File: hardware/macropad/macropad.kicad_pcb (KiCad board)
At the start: 2 copper layers, 13 parts, among them J2 Conn_01x04_Pin, SW1 SW_Push, SW2 SW_Push, SW3 SW_Push, SW4 SW_Push, SW5 SW_Push, SW6 SW_Push, SW7 SW_Push, SW8 SW_Push, SW9 SW_Push, U1 NRF24L01_Breakout, U2 AP2112K-3.3, U3 STM32F103C8Tx

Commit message: schematic halfass done
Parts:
- added C10: 10u, Capacitor_SMD:C_0805_2012Metric, F.Cu at (42.5, 65.8)
- added C11: 12p, Capacitor_SMD:C_0805_2012Metric, F.Cu at (42.5, 68.8)
- added C12: 100n, Capacitor_SMD:C_0805_2012Metric, F.Cu at (42.5, 71.8)
- added C13: 1u, Capacitor_SMD:C_0805_2012Metric, F.Cu at (42.5, 74.8)
- added C14: 100n, Capacitor_SMD:C_0805_2012Metric, F.Cu at (47.0, 65.8)
- added C15: 12p, Capacitor_SMD:C_0805_2012Metric, F.Cu at (47.0, 68.8)
- added C16: 100n, Capacitor_SMD:C_0805_2012Metric, F.Cu at (47.0, 71.8)
- added C17: 100n, Capacitor_SMD:C_0805_2012Metric, F.Cu at (47.0, 74.8)
- added C18: 1u, Capacitor_SMD:C_0805_2012Metric, F.Cu at (51.4, 65.8)
- added C19: 100n, Capacitor_SMD:C_0805_2012Metric, F.Cu at (51.4, 68.8)
- added C20: 100n, Capacitor_SMD:C_0805_2012Metric, F.Cu at (51.4, 71.8)
- added C21: 10u, Capacitor_SMD:C_0805_2012Metric, F.Cu at (51.4, 74.8)
- added J1: Conn_01x04_Pin, Connector_PinHeader_2.54mm:PinHeader_1x04_P2.54mm_Horizontal, F.Cu at (85.9, 52.3)
- added J3: Conn_02x03_Counter_Clockwise, Connector_PinHeader_2.54mm:PinHeader_1x04_P2.54mm_Vertical, F.Cu at (108.5, 116.6)
- added J4: display(4x1), Connector_PinHeader_2.54mm:PinHeader_1x04_P2.54mm_Vertical, F.Cu at (108.5, 101.9)
- added J5: enc1, Connector_PinHeader_2.54mm:PinHeader_1x05_P2.54mm_Horizontal, F.Cu at (121.9, 101.9)
- added J6: enc2, Connector_PinHeader_2.54mm:PinHeader_1x05_P2.54mm_Horizontal, F.Cu at (85.9, 37.6)
- added J7: Conn_01x04_Pin, Connector_PinHeader_2.54mm:PinHeader_1x04_P2.54mm_Horizontal, F.Cu at (42.6, 54.4)
- added J8: USB_A, Connector_USB:USB_A_Connfly_DS1095, F.Cu at (27.5, 54.2)
- added J9: Conn_02x03_Counter_Clockwise, Connector_PinHeader_2.54mm:PinHeader_2x03_P2.54mm_Vertical, F.Cu at (55.9, 66.6)
- added R11: 1.5K, Resistor_SMD:R_0805_2012Metric, F.Cu at (34.3, 69.7)
- added R12: 10k, Resistor_SMD:R_0805_2012Metric, F.Cu at (34.3, 72.7)
- added SW10: SW_Push, keyswitches:Kailh_socket_MX, F.Cu at (75.4, 43.4)
- added SW11: SW_Push, keyswitches:Kailh_socket_MX, F.Cu at (75.4, 59.5)
- added SW12: SW_Push, Button_Switch_SMD:SW_DIP_SPSTx01_Slide_6.7x4.1mm_W6.73mm_P2.54mm_LowProfile_JPin, F.Cu at (26.8, 71.1)
- added U4: AP2112K-3.3, Package_TO_SOT_SMD:SOT-23-5, F.Cu at (56.2, 59.0)
- added U5: STM32F103C8Tx, Package_QFP:LQFP-48_7x7mm_P0.5mm, F.Cu at (58.3, 41.0)
- added U6: NRF24L01_Breakout, RF_Module:nRF24L01_Breakout, F.Cu at (24.3, 38.1)
- added Y1: 8Mhz, Crystal:Crystal_SMD_3225-4Pin_3.2x2.5mm, F.Cu at (56.3, 54.4)
- J2: value Conn_01x04_Pin -> USB_B_Micro; footprint Connector:Tag-Connect_TC2030-IDC-NL_2x03_P1.27mm_Vertical -> Connector_PinHeader_2.54mm:PinHeader_1x04_P2.54mm_Horizontal
- SW1: value SW_Push -> SW_SPDT
- U1: value NRF24L01_Breakout -> AP2112K-3.3; footprint RF_Module:nRF24L01_Breakout -> Package_TO_SOT_SMD:SOT-23-5
- U2: value AP2112K-3.3 -> STM32F103C8Tx; footprint Package_TO_SOT_SMD:SOT-23-5 -> Package_QFP:LQFP-48_7x7mm_P0.5mm
- U3: value STM32F103C8Tx -> NRF24L01_Breakout; footprint Package_QFP:LQFP-48_7x7mm_P0.5mm -> RF_Module:nRF24L01_Breakout
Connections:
- J2 pad 1: +3.3V -> VBUS
- J2 pad 2: /SWDIO -> /USB_D-
- J2 pad 3: /SWCLK -> /USB_D+
- J2 pad 4: GND -> unconnected-(J2-ID-Pad4)
- SW1 pad 1: GND -> /BAT_OUT_ON
- SW1 pad 2: /K1 -> /BAT_OUT
- SW2 pad 1: GND -> /NRST
- SW2 pad 2: /K2 -> GND
- SW3 pad 2: /K4 -> /K1
- SW4 pad 2: /K5 -> /K4
- SW5 pad 2: /K6 -> /K7
- SW6 pad 2: /K3 -> /K2
- SW7 pad 2: /K7 -> /K5
- SW9 pad 2: /K9 -> /K3
- U1 pad 1: GND -> VDD
- U1 pad 2: +3.3V -> GND
- U1 pad 3: /PB1 -> unconnected-(U1-EN-Pad3)
- U1 pad 4: /PB0 -> unconnected-(U1-NC-Pad4)
- U1 pad 5: /PA5 -> +3.3V
- U2 pad 1: VDD -> unconnected-(U2-VBAT-Pad1)
- U2 pad 2: GND -> /K1
- U2 pad 3: unconnected-(U2-EN-Pad3) -> /K2
- U2 pad 4: unconnected-(U2-NC-Pad4) -> /K3
- U2 pad 5: +3.3V -> unconnected-(U2-PD0-Pad5)
- U3 pad 1: unconnected-(U3-VBAT-Pad1) -> GND
- U3 pad 2: /K1 -> +3.3V
- U3 pad 3: /K2 -> /PB1
- U3 pad 4: /K3 -> /PB0
- U3 pad 5: unconnected-(U3-PD0-Pad5) -> /PA5
- U3 pad 6: unconnected-(U3-PD1-Pad6) -> /PA7
- U3 pad 7: unconnected-(U3-NRST-Pad7) -> /PA6
- U3 pad 8: GND -> /PB10

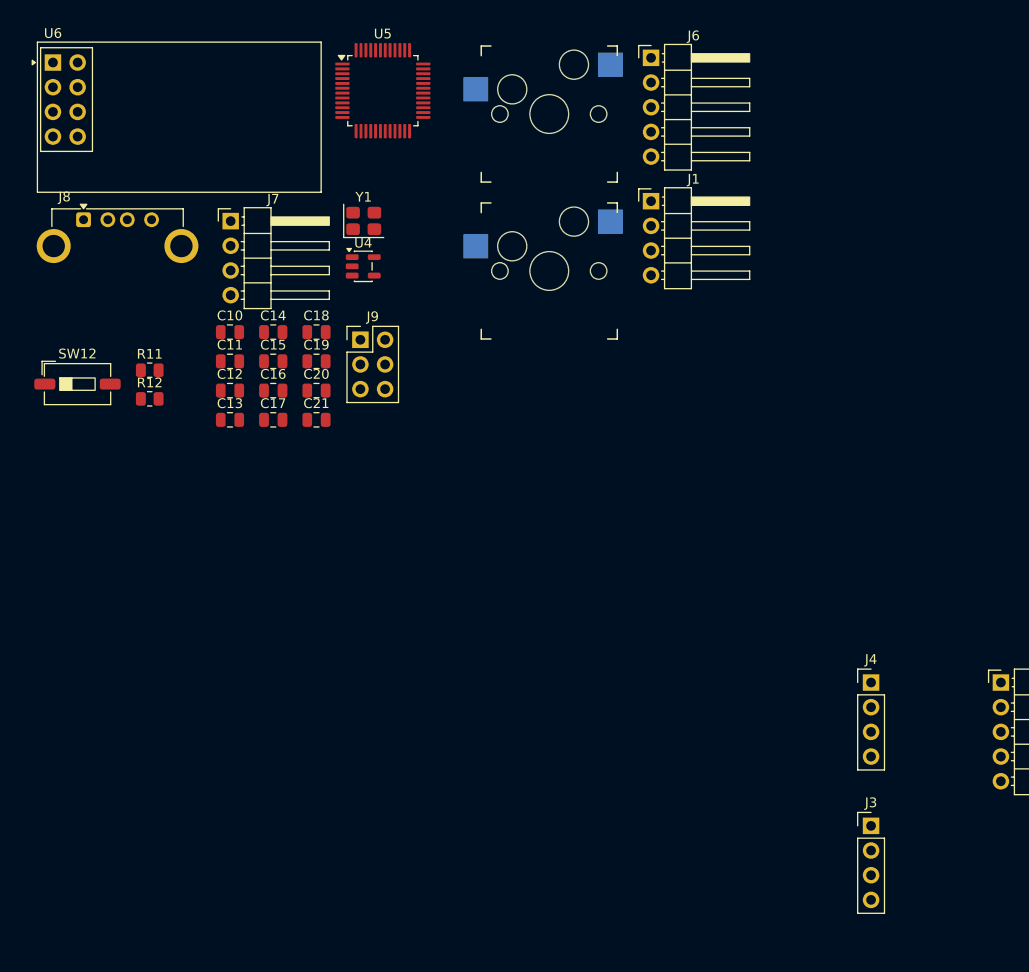
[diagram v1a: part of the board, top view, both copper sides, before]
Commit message: updated footprints
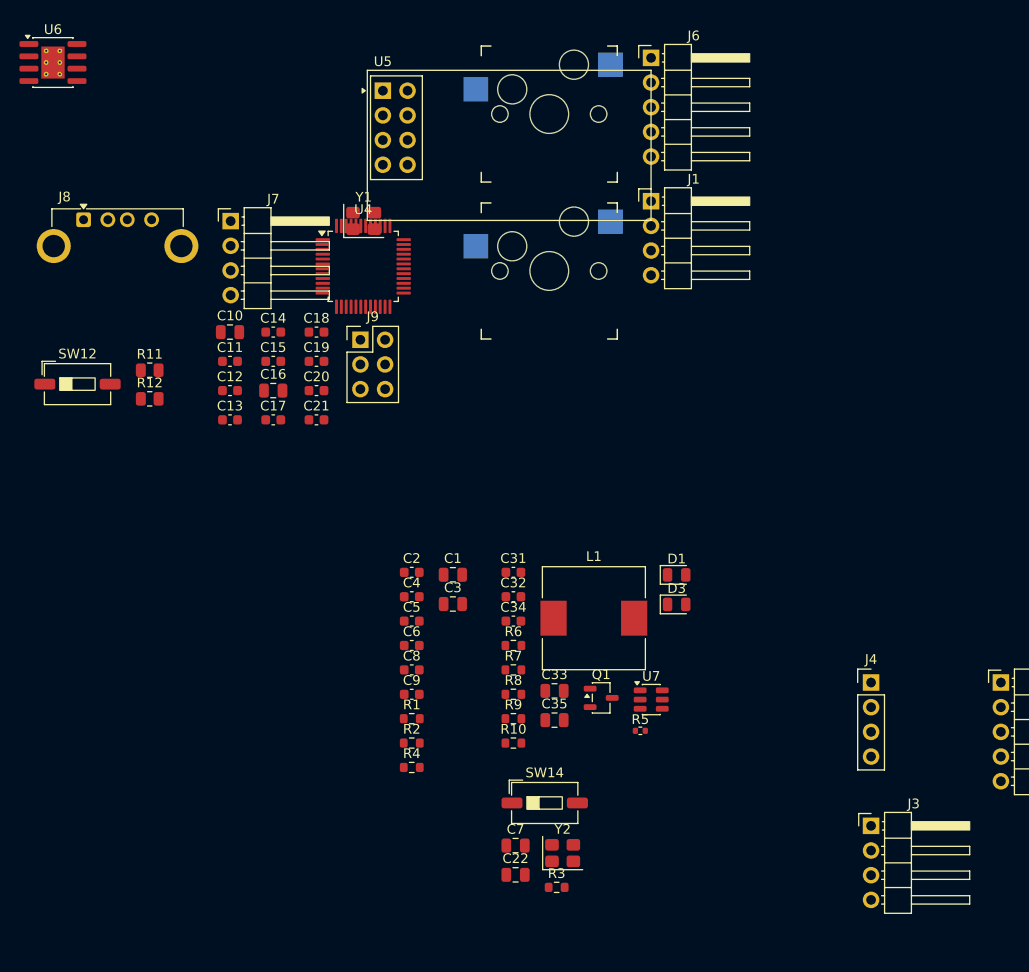
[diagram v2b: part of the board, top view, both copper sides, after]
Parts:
- added C1: 10u, Capacitor_SMD:C_0805_2012Metric, F.Cu at (65.5, 90.8)
- added C2: 100n, Capacitor_SMD:C_0603_1608Metric, F.Cu at (61.2, 90.5)
- added C22: 10u, Capacitor_SMD:C_0805_2012Metric, F.Cu at (71.9, 121.6)
- added C3: 10u, Capacitor_SMD:C_0805_2012Metric, F.Cu at (65.5, 93.8)
- added C31: 0.1u, Capacitor_SMD:C_0603_1608Metric, F.Cu at (71.7, 90.5)
- added C32: 0.1u, Capacitor_SMD:C_0603_1608Metric, F.Cu at (71.7, 93.0)
- added C33: 10u, Capacitor_SMD:C_0805_2012Metric, F.Cu at (75.9, 102.7)
- added C34: 4.7u, Capacitor_SMD:C_0603_1608Metric, F.Cu at (71.7, 95.5)
- added C35: 10u, Capacitor_SMD:C_0805_2012Metric, F.Cu at (75.9, 105.7)
- added C4: 100n, Capacitor_SMD:C_0603_1608Metric, F.Cu at (61.2, 93.0)
- added C5: 100n, Capacitor_SMD:C_0603_1608Metric, F.Cu at (61.2, 95.5)
- added C6: 100n, Capacitor_SMD:C_0603_1608Metric, F.Cu at (61.2, 98.0)
- added C7: 10u, Capacitor_SMD:C_0805_2012Metric, F.Cu at (71.9, 118.6)
- added C8: 100n, Capacitor_SMD:C_0603_1608Metric, F.Cu at (61.2, 100.6)
- added C9: 100n, Capacitor_SMD:C_0603_1608Metric, F.Cu at (61.2, 103.1)
- added D1: LED, LED_SMD:LED_0805_2012Metric, F.Cu at (88.5, 90.8)
- added D3: LED, LED_SMD:LED_0805_2012Metric, F.Cu at (88.5, 93.8)
- added L1: 2.2uH, Inductor_SMD:L_10.4x10.4_H4.8, F.Cu at (80.0, 95.2)
- added Q1: Q_PMOS, Package_TO_SOT_SMD:SOT-23-3, F.Cu at (80.7, 103.4)
- added R1: 5.1k, Resistor_SMD:R_0603_1608Metric, F.Cu at (61.2, 105.6)
- added R10: 100, Resistor_SMD:R_0603_1608Metric, F.Cu at (71.7, 108.1)
- added R2: 1.5k, Resistor_SMD:R_0603_1608Metric, F.Cu at (61.2, 108.1)
- added R3: 1.5K, Resistor_SMD:R_0603_1608Metric, F.Cu at (76.1, 122.9)
- added R4: 5.1k, Resistor_SMD:R_0603_1608Metric, F.Cu at (61.2, 110.6)
- added R5: 10k, Resistor_SMD:R_0402_1005Metric, F.Cu at (84.7, 106.8)
- added R6: 1k, Resistor_SMD:R_0603_1608Metric, F.Cu at (71.7, 98.0)
- added R7: 1k, Resistor_SMD:R_0603_1608Metric, F.Cu at (71.7, 100.6)
- added R8: 1.2k, Resistor_SMD:R_0603_1608Metric, F.Cu at (71.7, 103.1)
- added R9: 1k, Resistor_SMD:R_0603_1608Metric, F.Cu at (71.7, 105.6)
- added SW14: SW_Push, Button_Switch_SMD:SW_DIP_SPSTx01_Slide_6.7x4.1mm_W6.73mm_P2.54mm_LowProfile_JPin, F.Cu at (74.9, 114.3)
- added U7: DW01A, Package_TO_SOT_SMD:SOT-23-6, F.Cu at (85.9, 103.6)
- added Y2: 8Mhz, Crystal:Crystal_SMD_3225-4Pin_3.2x2.5mm, F.Cu at (76.8, 119.4)
- C10: value 10u -> 1u
- C11, C15: value 12p -> 18p; footprint Capacitor_SMD:C_0805_2012Metric -> Capacitor_SMD:C_0603_1608Metric
- C12, C14, C19, C20: footprint Capacitor_SMD:C_0805_2012Metric -> Capacitor_SMD:C_0603_1608Metric
- C13: value 1u -> 100n; footprint Capacitor_SMD:C_0805_2012Metric -> Capacitor_SMD:C_0603_1608Metric
- C16: value 100n -> 1u
- C17: value 100n -> 18p; footprint Capacitor_SMD:C_0805_2012Metric -> Capacitor_SMD:C_0603_1608Metric
- C18: value 1u -> 18p; footprint Capacitor_SMD:C_0805_2012Metric -> Capacitor_SMD:C_0603_1608Metric
- C21: value 10u -> 100n; footprint Capacitor_SMD:C_0805_2012Metric -> Capacitor_SMD:C_0603_1608Metric
- J1: value Conn_01x04_Pin -> SWD
- J2: value USB_B_Micro -> USB_C_Receptacle
- J3: value Conn_02x03_Counter_Clockwise -> Conn_01x04_Pin; footprint Connector_PinHeader_2.54mm:PinHeader_1x04_P2.54mm_Vertical -> Connector_PinHeader_2.54mm:PinHeader_1x04_P2.54mm_Horizontal
- J5: value enc1 -> USB_A
- SW1: value SW_SPDT -> SW_Push
- SW10: value SW_Push -> SW_SPDT
- SW12: value SW_Push -> Enc1
- U4: value AP2112K-3.3 -> STM32F103C8Tx; footprint Package_TO_SOT_SMD:SOT-23-5 -> Package_QFP:LQFP-48_7x7mm_P0.5mm
- U5: value STM32F103C8Tx -> NRF24L01_Breakout; footprint Package_QFP:LQFP-48_7x7mm_P0.5mm -> RF_Module:nRF24L01_Breakout
- U6: value NRF24L01_Breakout -> TP4056-42-ESOP8; footprint RF_Module:nRF24L01_Breakout -> Package_SO:SOIC-8-1EP_3.9x4.9mm_P1.27mm_EP2.41x3.3mm_ThermalVias
- Y1: value 8Mhz -> 8Mhz C_L=12pF
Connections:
- C10 pad 1: +3.3V -> VBUS_DGL
- C10 pad 2: GND -> GND_DGL
- C11 pad 1: /dongle/HSE_IN -> /dongle/HSE_IN_DGL
- C11 pad 2: GND -> GND_DGL
- C12 pad 1: +3.3V -> +3.3V_DGL
- C12 pad 2: GND -> GND_DGL
- C13 pad 1: VDD -> +3.3V_DGL
- C13 pad 2: GND -> GND_DGL
- C14 pad 1: +3.3V -> +3.3V_DGL
- C14 pad 2: GND -> GND_DGL
- C15 pad 1: /dongle/HSE_OUT -> /dongle/HSE_OUT_DGL
- C15 pad 2: GND -> GND_DGL
- C16 pad 1: +3.3V -> +3.3V_DGL
- C16 pad 2: GND -> GND_DGL
- C17 pad 1: +3.3V -> /HSE_IN
- C17 pad 2: GND -> GND_DGL
- C18 pad 1: +3.3V -> /HSE_OUT
- C18 pad 2: GND -> GND_DGL
- C19 pad 1: +3.3V -> +3.3V_DGL
- C19 pad 2: GND -> GND_DGL
- C20 pad 1: GND -> +3.3V_DGL
- C20 pad 2: /dongle/NRST -> GND_DGL
- C21 pad 1: +3.3V -> GND_DGL
- C21 pad 2: GND -> /dongle/NRST_DGL
- J2 pad 1: VBUS -> (no net)
- J2 pad 2: /USB_D- -> (no net)
- J2 pad 3: /USB_D+ -> (no net)
- J2 pad 4: unconnected-(J2-ID-Pad4) -> (no net)
- J3 pad 1: GND -> +3.3V_DGL
- J3 pad 2: /BOOT1 -> /dongle/SWDIO_DGL
- J3 pad 3: +3.3V -> /dongle/SWCLK_DGL
- J3 pad 4: +3.3V -> GND_DGL
- J5 pad 1: GND -> VBUS_DGL
- J5 pad 2: +3.3V -> /dongle/USB_D-_DGL
- J5 pad 3: /ENC1SW_PA2 -> /dongle/USB_D+_DGL
- J5 pad 4: /ENC1DT_PA0 -> GND_DGL
- J5 pad 5: /ENC1CLK_PA1 -> GND_DGL
- SW1 pad 1: /BAT_OUT_ON -> GND
- SW1 pad 2: /BAT_OUT -> /K1
- SW10 pad 1: GND -> /BAT_OUT_ON
- SW10 pad 2: /K6 -> /BAT_OUT
- SW11 pad 1: GND -> /NRST
- SW11 pad 2: /K9 -> GND
- SW12 pad 1: /dongle/NRST -> (no net)
- SW12 pad 2: GND -> (no net)
- SW2 pad 1: /NRST -> GND
- SW2 pad 2: GND -> /K2
- SW3 pad 2: /K1 -> /K3
- SW5 pad 2: /K7 -> /K5
- SW6 pad 2: /K2 -> /K6
- SW7 pad 2: /K5 -> /K7
- SW9 pad 2: /K3 -> /K9
- U1 pad 1: VDD -> VBUS_DGL
- U1 pad 2: GND -> GND_DGL
- U1 pad 3: unconnected-(U1-EN-Pad3) -> VBUS_DGL
- U1 pad 5: +3.3V -> +3.3V_DGL
- U2 pad 1: unconnected-(U2-VBAT-Pad1) -> +3.3V
- U2 pad 2: /K1 -> unconnected-(U2-PC13-Pad2)
- U2 pad 20: /BOOT1 -> GND
- U2 pad 22: unconnected-(U2-PB11-Pad22) -> /K6
- U2 pad 25: unconnected-(U2-PB12-Pad25) -> /K7
- U2 pad 26: unconnected-(U2-PB13-Pad26) -> /K8
- U2 pad 27: unconnected-(U2-PB14-Pad27) -> /K9
- U2 pad 3: /K2 -> unconnected-(U2-PC14-Pad3)
- U2 pad 39: unconnected-(U2-PB3-Pad39) -> /K1
- U2 pad 4: /K3 -> unconnected-(U2-PC15-Pad4)
- U2 pad 40: unconnected-(U2-PB4-Pad40) -> /K2
- U2 pad 41: unconnected-(U2-PB5-Pad41) -> /K3
- U2 pad 44: /BOOT0 -> GND
- U2 pad 45: unconnected-(U2-PB8-Pad45) -> /K4
- U2 pad 46: unconnected-(U2-PB9-Pad46) -> /K5
- U2 pad 5: unconnected-(U2-PD0-Pad5) -> /HSE_IN
- U2 pad 6: unconnected-(U2-PD1-Pad6) -> /HSE_OUT
- U4 pad 1: VDD -> +3.3V_DGL
- U4 pad 2: GND -> unconnected-(U4-PC13-Pad2)
- U4 pad 5: +3.3V -> /dongle/HSE_IN_DGL
- U5 pad 1: +3.3V -> GND_DGL
- U5 pad 2: unconnected-(U5-PC13-Pad2) -> +3.3V_DGL
- U5 pad 3: unconnected-(U5-PC14-Pad3) -> /dongle/PB1_DGL
- U5 pad 4: unconnected-(U5-PC15-Pad4) -> /dongle/PB0_DGL
- U5 pad 5: /dongle/HSE_IN -> /dongle/PA5_DGL
- U5 pad 6: /dongle/HSE_OUT -> /dongle/PA7_DGL
- U5 pad 7: /dongle/NRST -> /dongle/PA6_DGL
- U5 pad 8: GND -> /dongle/PB10_DGL
- U6 pad 2: +3.3V -> Net-(U6-PROG)
- U6 pad 3: /dongle/PB1 -> GND
- U6 pad 4: /dongle/PB0 -> +5V
- U6 pad 5: /dongle/PA5 -> /Power/B+
- U6 pad 6: /dongle/PA7 -> Net-(U6-~{STDBY})
- U6 pad 7: /dongle/PA6 -> Net-(U6-~{CHRG})
- U6 pad 8: /dongle/PB10 -> +5V
- Y1 pad 1: /dongle/HSE_IN -> /HSE_IN
- Y1 pad 2: GND -> GND_DGL
- Y1 pad 3: /dongle/HSE_OUT -> /HSE_OUT
- Y1 pad 4: GND -> GND_DGL

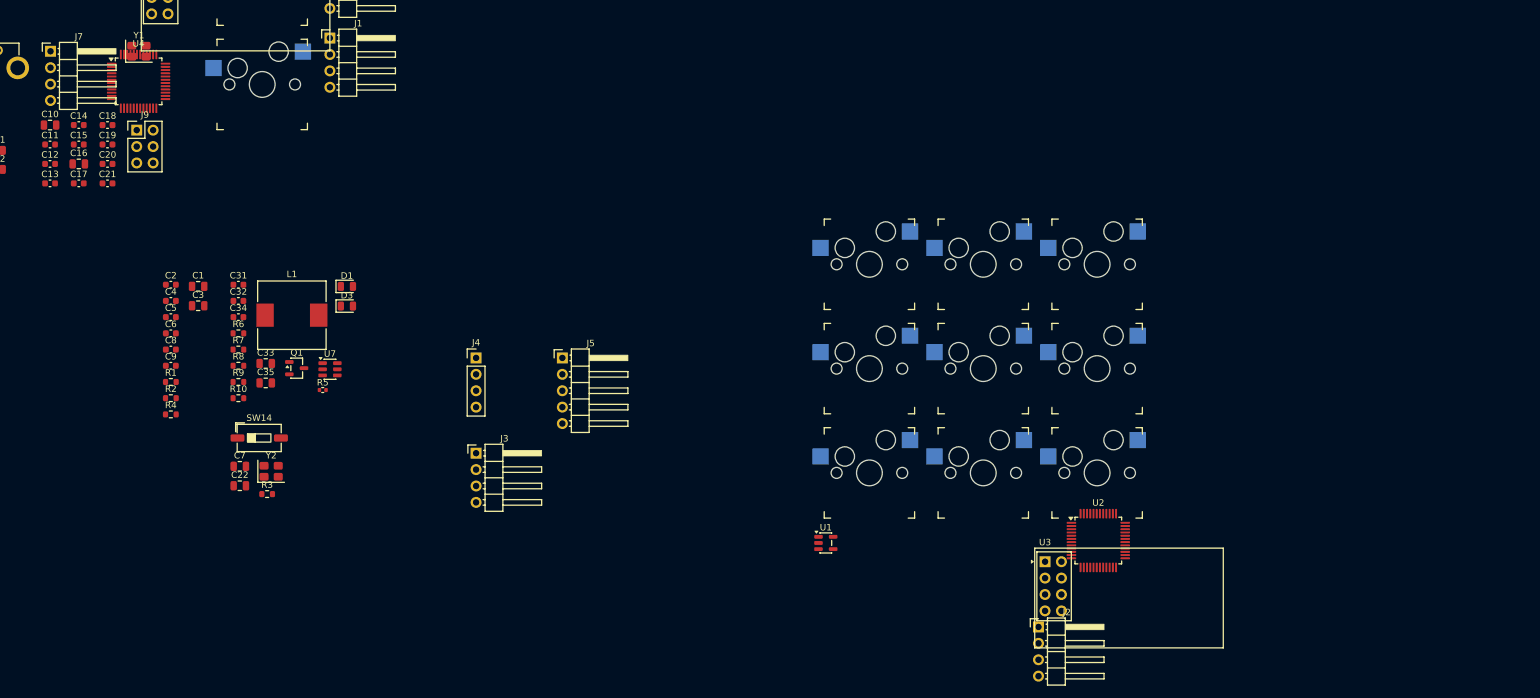
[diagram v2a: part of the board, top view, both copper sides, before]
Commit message: added usb-c receptacle footprint
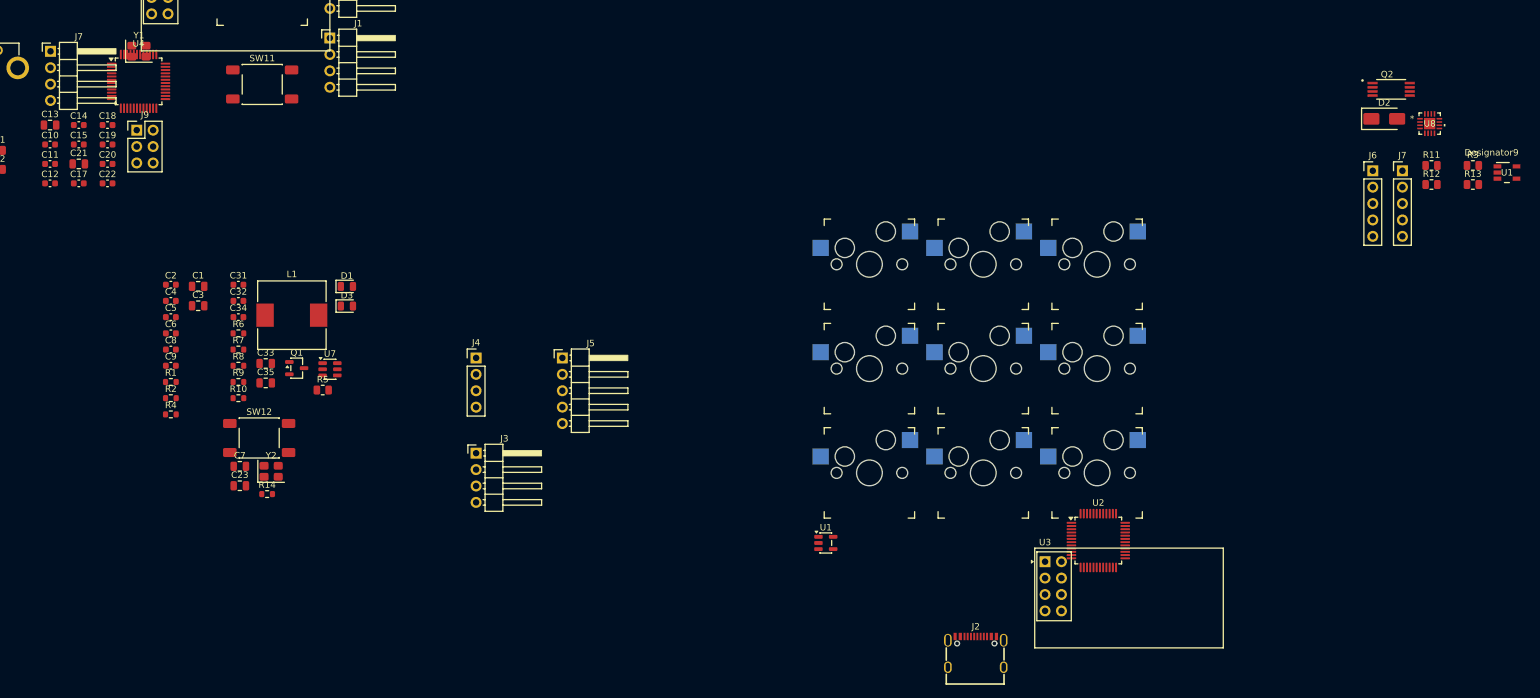
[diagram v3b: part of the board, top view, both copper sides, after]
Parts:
- added D2: D_Schottky, Diode_SMD:D_SMA, F.Cu at (249.1, 64.8)
- added J6: Enc2, Connector_PinHeader_2.54mm:PinHeader_1x05_P2.54mm_Vertical, F.Cu at (247.3, 72.9)
- added J7: Enc1, Connector_PinHeader_2.54mm:PinHeader_1x05_P2.54mm_Vertical, F.Cu at (251.9, 72.9)
- added Q2: FS8205A, FS8205A:SOP65P640X120-8N, F.Cu at (250.2, 60.3)
- added R11: 10k, Resistor_SMD:R_0805_2012Metric, F.Cu at (256.4, 72.1)
- added R12: 10k, Resistor_SMD:R_0805_2012Metric, F.Cu at (256.4, 75.0)
- added R13: 10k, Resistor_SMD:R_0805_2012Metric, F.Cu at (262.8, 75.0)
- added R3: 10k, Resistor_SMD:R_0805_2012Metric, F.Cu at (262.8, 72.1)
- added U1: LP2992IM5-3.3/NOPB, LP2992:DBV0005A_M, F.Cu at (268.1, 73.2)
- added U8: RT8010AGQW, RT8010:WQFN16_RT8010_RIT-M, F.Cu at (256.2, 65.6)
- C21: renamed from C16; value 1u -> 2.2u
- J2: footprint Connector_PinHeader_2.54mm:PinHeader_1x04_P2.54mm_Horizontal -> usbc:TYPE-C-SMD_U263-163N-4GS1735
- R5: footprint Resistor_SMD:R_0402_1005Metric -> Resistor_SMD:R_0805_2012Metric
- SW11: footprint keyswitches:Kailh_socket_MX -> Button_Switch_SMD:SW_Push_1P1T_NO_E-Switch_TL3301NxxxxxG
- SW12: renamed from SW14; footprint Button_Switch_SMD:SW_DIP_SPSTx01_Slide_6.7x4.1mm_W6.73mm_P2.54mm_LowProfile_JPin -> Button_Switch_SMD:SW_Push_1P1T_NO_E-Switch_TL3301NxxxxxG
- moved J2 10.5 mm to (185.9, 147.4)
- renumbered C11 to C10, C12 to C11, C13 to C12, C10 to C13, C21 to C22, C22 to C23, R3 to R14
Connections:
- U2 pad 20: GND -> /BOOT1
- U2 pad 44: GND -> /BOOT0
- U4 pad 20: GND_DGL -> /dongle/BOOT1_DGL
- U4 pad 44: GND_DGL -> /dongle/BOOT0_DGL
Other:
- board outline added: 6.5 x 0.7 mm
